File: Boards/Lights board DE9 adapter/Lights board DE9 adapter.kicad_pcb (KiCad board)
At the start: 2 copper layers, 18.6 x 64.6 mm, 5 parts, among them J3 light connector, J4 DE9_Socket_MountingHoles, J5 Conn_02x08_Odd_Even, J6 Conn_02x04_Odd_Even

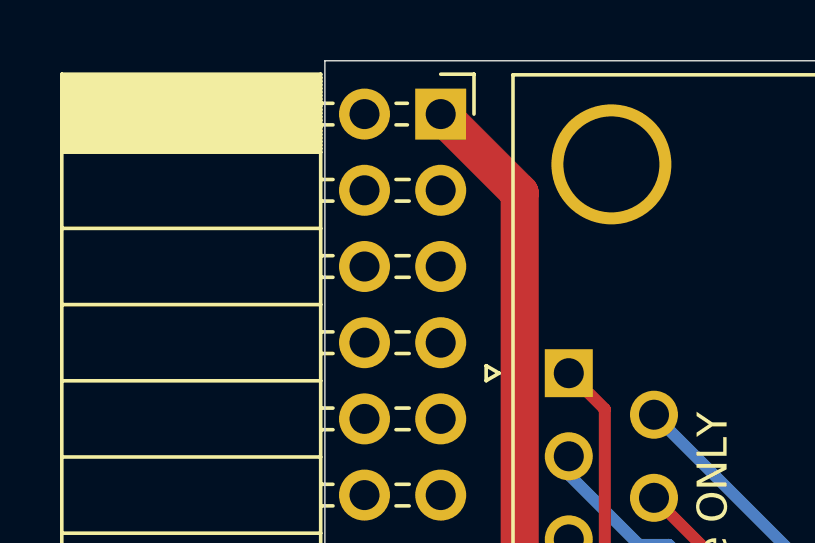
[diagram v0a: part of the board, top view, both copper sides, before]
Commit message: changes from ordering lights de9 adapter
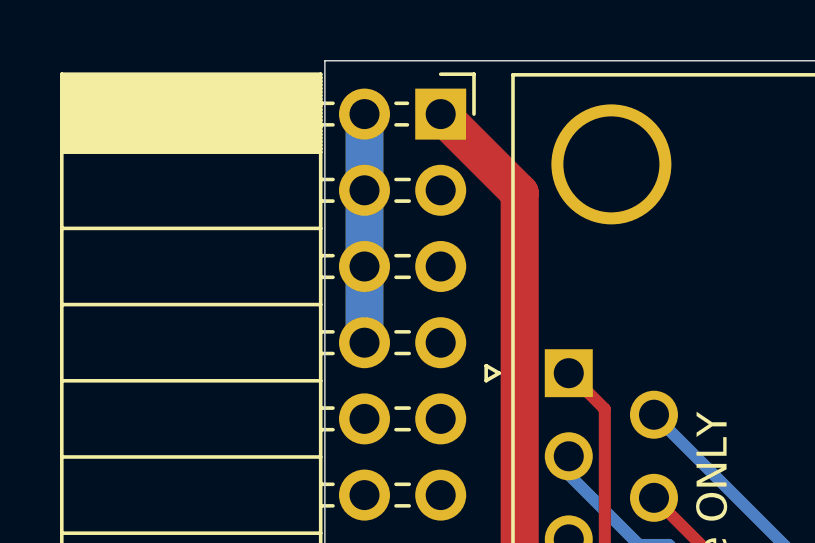
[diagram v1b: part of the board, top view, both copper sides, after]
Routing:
- net 24R: track 0.00 -> 7.62 mm
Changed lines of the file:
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@@
+	)
+	(segment
+		(start 111.3536 22.5044)
+		(end 111.3536 25.0444)
+		(width 1.27)
+		(layer "B.Cu")
+		(net 1)
+	)
+	(segment
+		(start 111.3536 19.9644)
+		(end 111.3536 22.5044)
+		(width 1.27)
+		(layer "B.Cu")
+		(net 1)
+	)
+	(segment
+		(start 111.3536 25.0444)
+		(end 111.3536 27.5844)
+		(width 1.27)
+		(layer "B.Cu")
+		(net 1)
 	)
 	(segment
